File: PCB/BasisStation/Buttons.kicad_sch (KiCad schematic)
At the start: 3 parts, among them SW2 RESET_BUTTON

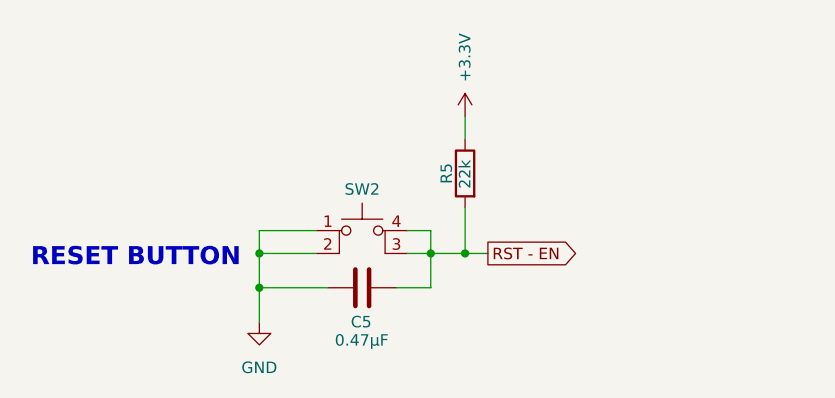
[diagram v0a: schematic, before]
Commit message: Schaltplan angepasst
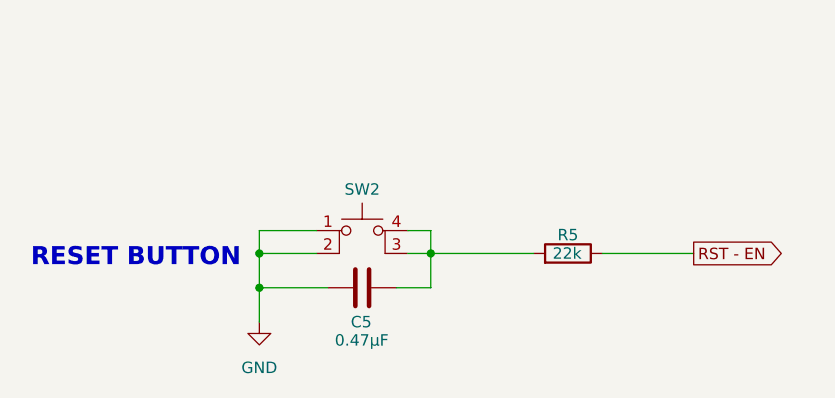
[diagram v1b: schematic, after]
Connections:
- net +3.3V is gone; now on net RST - EN: R5.1
- net RST - EN: no longer C5.2, R5.2, SW2.3 (K), SW2.4 (A)
- new net: C5.2, R5.2, SW2.3 (K), SW2.4 (A)
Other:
- moved on the sheet: R5
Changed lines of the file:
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@@
-	)
-	(junction
-		(at 109.22 120.65)
-		(diameter 0)
-		(color 0 0 0 0)
 	)
 	(junction
@@
 	(wire
 		(pts
+			(xy 105.41 120.65) (xy 116.84 120.65)
+		)
+		(stroke
+			(width 0)
+			(type default)
+		)
+	)
+	(wire
+		(pts
 			(xy 86.36 118.11) (xy 86.36 120.65)
 		)
@@
 	(wire
 		(pts
-			(xy 109.22 105.41) (xy 109.22 107.95)
-		)
-		(stroke
-			(width 0)
-			(type default)
-		)
-	)
-	(wire
-		(pts
 			(xy 102.87 118.11) (xy 105.41 118.11)
 		)
@@
 	(wire
 		(pts
-			(xy 109.22 120.65) (xy 111.76 120.65)
+			(xy 124.46 120.65) (xy 134.62 120.65)
 		)
 		(stroke
@@
 	(wire
 		(pts
-			(xy 105.41 120.65) (xy 109.22 120.65)
-		)
-		(stroke
-			(width 0)
-			(type default)
-		)
-	)
-	(wire
-		(pts
 			(xy 105.41 124.46) (xy 105.41 120.65)
-		)
-		(stroke
-			(width 0)
-			(type default)
-		)
-	)
-	(wire
-		(pts
-			(xy 109.22 115.57) (xy 109.22 120.65)
 		)
 		(stroke
@@
 	(global_label "RST - EN"
 		(shape output)
-		(at 111.76 120.65 0)
+		(at 134.62 120.65 0)
 		(fields_autoplaced yes)
 		(effects
@@
 		)
 		(property "Intersheetrefs" "${INTERSHEET_REFS}"
-			(at 124.1794 120.65 0)
+			(at 147.0394 120.65 0)
 			(effects
 				(font
@@
 		(lib_name "R_2")
 		(lib_id "Device:R")
-		(at 109.22 111.76 0)
-		(mirror y)
+		(at 120.65 120.65 270)
+		(mirror x)
 		(unit 1)
 		(exclude_from_sim no)
@@
 		(dnp no)
 		(property "Reference" "R5"
-			(at 106.426 111.76 90)
+			(at 120.65 117.856 90)
 			(do_not_autoplace yes)
 			(effects
@@
 		)
 		(property "Value" "22k"
-			(at 109.22 110.236 90)
+			(at 122.174 120.65 90)
 			(effects
 				(font
@@
 		)
 		(property "Footprint" "Resistor_THT:R_Axial_Power_L60.0mm_W14.0mm_P66.04mm"
-			(at 110.998 111.76 90)
+			(at 120.65 122.428 90)
 			(effects
 				(font
@@
 		)
 		(property "Datasheet" "chrome-extension://efaidnbmnnnibpcajpcglclefindmkaj/https://www.mouser.de/datasheet/2/418/3/NG_CS_1309350_PASSIVE_COMPONENT_0807-1235468.pdf"
-			(at 109.22 111.76 0)
+			(at 120.65 120.65 0)
 			(effects
 				(font
@@
 		)
 		(property "Description" "Resistor"
-			(at 109.22 111.76 0)
+			(at 120.65 120.65 0)
 			(effects
 				(font
@@
 					(unit 1)
 				)
-			)
-		)
-	)
-	(symbol
-		(lib_id "power:VCC")
-		(at 109.22 105.41 0)
-		(unit 1)
-		(exclude_from_sim no)
-		(in_bom yes)
-		(on_board yes)
-		(dnp no)
-		(fields_autoplaced yes)
-		(property "Reference" "#PWR019"
-			(at 109.22 109.22 0)
-			(effects
-				(font
-					(size 1.27 1.27)
-				)
-				(hide yes)
-			)
-		)
-		(property "Value" "+3.3V"
-			(at 109.2199 101.6 90)
-			(effects
-				(font
-					(size 1.27 1.27)
-				)
-				(justify left)
-			)
-		)
-		(property "Footprint" ""
-			(at 109.22 105.41 0)
-			(effects
-				(font
-					(size 1.27 1.27)
-				)
-				(hide yes)
-			)
-		)
-		(property "Datasheet" ""
-			(at 109.22 105.41 0)
-			(effects
-				(font
-					(size 1.27 1.27)
-				)
-				(hide yes)
-			)
-		)
-		(property "Description" "Power symbol creates a global label with name \"VCC\""
-			(at 109.22 105.41 0)
-			(effects
-				(font
-					(size 1.27 1.27)
-				)
-				(hide yes)
-			)
-		)
-		(pin "1"
-		)
-		(instances
-			(project "BasisStation"
-				(path "/cc03a18a-a128-4e00-a998-441923eeacd1/3a7cd9fc-3eb4-4108-a75f-b08dbde2a6f7"
-					(reference "#PWR019")
-					(unit 1)
-				)
